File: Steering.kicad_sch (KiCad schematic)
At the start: 0 parts

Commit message: Steering: Current sensing, STM32 core, dual CAN, LEDs, test points
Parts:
- added C56, C57, C58, C61, C62, C63, C64, C65, C67, C68, C69, C70, C71, C72: 100nF, Capacitor_SMD:C_0603_1608Metric, symbol Device:C
- added C59, C66: 4.7uF, Capacitor_SMD:C_0805_2012Metric, symbol Device:C
- added C60: 1uF, Capacitor_SMD:C_0603_1608Metric, symbol Device:C
- added C73, C74, C75, C76: 22pF, Capacitor_SMD:C_0603_1608Metric, symbol Device:C
- added C85: 100nF, symbol Device:C
- added C86: 100nF, Package_SO:SOIC-8_3.9x4.9mm_P1.27mm, symbol Device:C
- added C87: 220uF, symbol Device:C
- added D11, D13, D14, D15: LED, LED_THT:LED_D3.0mm, symbol Device:LED
- added D12: LED, Resistor_SMD:R_0603_1608Metric, symbol Device:LED
- added FB2: 600R@100MHz, Inductor_SMD:L_0603_1608Metric, symbol Device:FerriteBead_Small
- added J10: Conn_01x03, Connector_PinHeader_2.54mm:PinHeader_1x03_P2.54mm_Vertical, symbol Connector_Generic:Conn_01x03
- added J11: SWD, Connector_PinHeader_2.54mm:PinHeader_1x06_P2.54mm_Vertical, symbol Connector_Generic:Conn_01x06
- added J12: SERVO, Connector:Tag-Connect_TC2030-IDC-FP_2x03_P1.27mm_Vertical, symbol Connector_Generic:Conn_01x03
- added J13: Conn_01x13, Connector:Tag-Connect_TC2030-IDC-FP_2x03_P1.27mm_Vertical, symbol Connector_Generic:Conn_01x13
- added R39, R43, R46, R47, R48, R49: 10k, Resistor_SMD:R_0603_1608Metric, symbol Device:R
- added R40, R41, R42, R44, R45: 220, Resistor_SMD:R_0603_1608Metric, symbol Device:R
- added R50, R51: 120R, Resistor_SMD:R_0603_1608Metric, symbol Device:R
- added R52: 50m, Resistor_SMD:R_Shunt_Vishay_WSK2512_6332Metric_T1.19mm, symbol Device:R_Shunt
- added R58: 1k, Package_SO:TSSOP-20_4.4x6.5mm_P0.65mm, symbol Device:R
- added SW10: SW_Push, Button_Switch_THT:SW_PUSH_6mm, symbol Switch:SW_Push
- added SW11, SW12: 219-2MSTR, Button_Switch_SMD:SW_DIP_SPSTx02_Slide_6.7x6.64mm_W8.61mm_P2.54mm_LowProfile, symbol Switch:SW_DIP_x02
- added SW13, SW14: CVS-01TB, Button_Switch_SMD:SW_DIP_SPSTx01_Slide_Copal_CVS-01xB_W5.9mm_P1mm, symbol Switch:SW_DIP_x01
- added TP21: TestPoint, Package_TO_SOT_SMD:SOT-23-5, symbol Connector:TestPoint
- added U13: STM32F401RETx, Package_QFP:LQFP-64_10x10mm_P0.5mm, symbol MCU_ST_STM32F4:STM32F401RETx
- added U14, U15: MCP2515T-I/ST, Package_SO:TSSOP-20_4.4x6.5mm_P0.65mm, symbol Interface_CAN_LIN:MCP2515-xST
- added U16, U17: SN65HVD230, Package_SO:SOIC-8_3.9x4.9mm_P1.27mm, symbol Interface_CAN_LIN:SN65HVD230
- added U18: INA180A1, Package_TO_SOT_SMD:SOT-23-5, symbol Amplifier_Current:INA180A1
- added Y5, Y6: 16 MHz, Crystal:Crystal_SMD_3225-4Pin_3.2x2.5mm, symbol Device:Crystal_GND24
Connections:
- new net: U15.1 (TXCAN), U17.1 (D)
- new net: U15.2 (RXCAN), U17.4 (R)
- new net: SW12.2, U17.6 (CANL)
- new net: SW12.1, U17.7 (CANH)
- new net: R49.2, U17.8 (Rs)
- new net: R43.1, U13.60 (BOOT0)
- new net: C70.1, R47.1, U15.19 (~{RESET})
- new net: D13.2 (A), R42.2
- new net: R50.1, SW13.1
- new net: C57.2, C60.2, FB2.2, U13.13 (VREF+)
- new net: U14.1 (TXCAN), U16.1 (D)
- new net: U14.2 (RXCAN), U16.4 (R)
- new net: SW11.2, U16.6 (CANL)
- new net: SW11.1, U16.7 (CANH)
- new net: R48.2, U16.8 (Rs)
- new net: D12.2 (A), R41.2
- new net: C69.1, R46.1, U14.19 (~{RESET})
- new net: R51.1, SW14.1
- new net: R52.2, U18.3 (+)
- new net: R52.3, U18.4 (-)
- new net: D14.2 (A), R44.2
- new net: D11.2 (A), R40.2
- new net: C59.2, U13.30 (VCAP1)
- new net: D15.2 (A), R45.2
- new net +6V: C87.1, R52.1
- new net 3V3: C61.2, C62.2, C63.2, C64.1, C65.1, C66.1, C67.1, C68.1, C71.1, C72.1, C86.1, FB2.1, J11.1 (Pin_1), R39.1, R46.2, R47.2, U13.1 (VBAT), U13.19 (VDD), U13.32 (VDD), U13.48 (VDD), U13.64 (VDD), U14.20 (VDD), U15.20 (VDD), U16.3 (VCC), U17.3 (VCC), U18.5 (V+)
- new net CANH_A: R50.2, SW11.4
- new net CANH_B: R51.2, SW12.4
- new net CANL_A: SW11.3, SW13.2
- new net CANL_B: SW12.3, SW14.2
- new net GND: C56.2, C57.1, C58.1, C59.1, C60.1, C61.1, C62.1, C63.1, C64.2, C65.2, C66.2, C67.2, C68.2, C69.2, C70.2, C71.2, C72.2, C73.2, C74.2, C75.2, C76.2, C85.2, C86.2, C87.2, D11.1 (K), D12.1 (K), D13.1 (K), D14.1 (K), D15.1 (K), J10.3 (Pin_3), J11.3 (Pin_3), J12.3 (Pin_3), J13.1 (Pin_1), J13.2 (Pin_2), R43.2, R48.1, R49.1, SW10.1, U13.12 (VSSA), U13.18 (VSS), U13.31 (VSS), U13.47 (VSS), U13.63 (VSS), U14.10 (VSS), U15.10 (VSS), U16.2 (GND), U17.2 (GND), U18.2 (GND), Y5.2 (G), Y5.4 (G), Y6.2 (G), Y6.4 (G)
- new net OSC_ST_A1: C73.1, U14.9 (OSC1), Y5.1
- new net OSC_ST_A2: C75.1, U14.8 (OSC2), Y5.3
- new net OSC_ST_B1: C74.1, U15.8 (OSC2), Y6.1
- new net OSC_ST_B2: C76.1, U15.9 (OSC1), Y6.3
- new net RELAY_TX: J13.12 (Pin_12), U13.42 (PA9)
- new net SERVO_ISENSE: C85.1, R58.2, U13.9 (PC1)
- new net SERVO_PWM: J12.2 (Pin_2)
- new net SERVO_V+: J12.1 (Pin_1), R52.4
- new net SRV: J13.9 (Pin_9), U13.62 (PB9)
- new net ST_CAN_A_CS: U13.58 (PB6), U14.18 (~{CS})
- new net ST_CAN_A_INT: U13.43 (PA10), U14.13 (~{INT})
- new net ST_CAN_B_CS: U13.38 (PC7), U15.18 (~{CS})
- new net ST_CAN_B_INT: U13.57 (PB5), U15.13 (~{INT})
- new net ST_CAN_RX_A: J13.3 (Pin_3), U13.10 (PC2)
- new net ST_CAN_RX_B: J13.4 (Pin_4), U13.11 (PC3)
- new net ST_CAN_TX_A: J13.5 (Pin_5), U13.51 (PC10)
- new net ST_CAN_TX_B: J13.6 (Pin_6), U13.52 (PC11)
- new net ST_DEG_A: J13.7 (Pin_7), R41.1, U13.61 (PB8)
- new net ST_DEG_B: J13.8 (Pin_8), R40.1, U13.8 (PC0)
- new net ST_ERR: J13.13 (Pin_13), R42.1, U13.53 (PC12), U13.55 (PB3)
- new net ST_FL: J13.10 (Pin_10), R44.1, U13.29 (PB10)
- new net ST_FR: J13.11 (Pin_11), R45.1, U13.41 (PA8)
- new net ST_NRST: C58.2, J11.5 (Pin_5), U13.7 (NRST)
- new net ST_SELF_TEST: C56.1, R39.2, SW10.2, U13.2 (PC13)
- new net ST_SPI_MISO: U13.22 (PA6), U14.17 (SO), U15.17 (SO)
- new net ST_SPI_MOSI: U13.23 (PA7), U14.16 (SI), U15.16 (SI)
- new net ST_SPI_SCLK: U13.21 (PA5), U14.14 (SCK), U15.14 (SCK)
- new net ST_SWCLK: J11.2 (Pin_2), U13.49 (PA14)
- new net ST_SWDIO: J11.4 (Pin_4), U13.46 (PA13)
- new net ST_SWO: J11.6 (Pin_6), U13.56 (PB4)
- new net ST_UART_RX: J10.1 (Pin_1), U13.17 (PA3)
- new net ST_UART_TX: J10.2 (Pin_2), U13.16 (PA2)
- new net TP_SERVO_ISENSE: R58.1, TP21.1, U18.1
- no-connect marks 0 -> 38
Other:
- note added: "CAN A Interface"
- note added: "CAN B Interface"
- note added: "Connectors & Test Points"
- note added: "Current Sensing"
- note added: "I_mA = counts * 0.806 - offset Sample rate @ >=10KHz"
- note added: "Kelvin"
- note added: "Low ESR"
- note added: "STM Breakout"

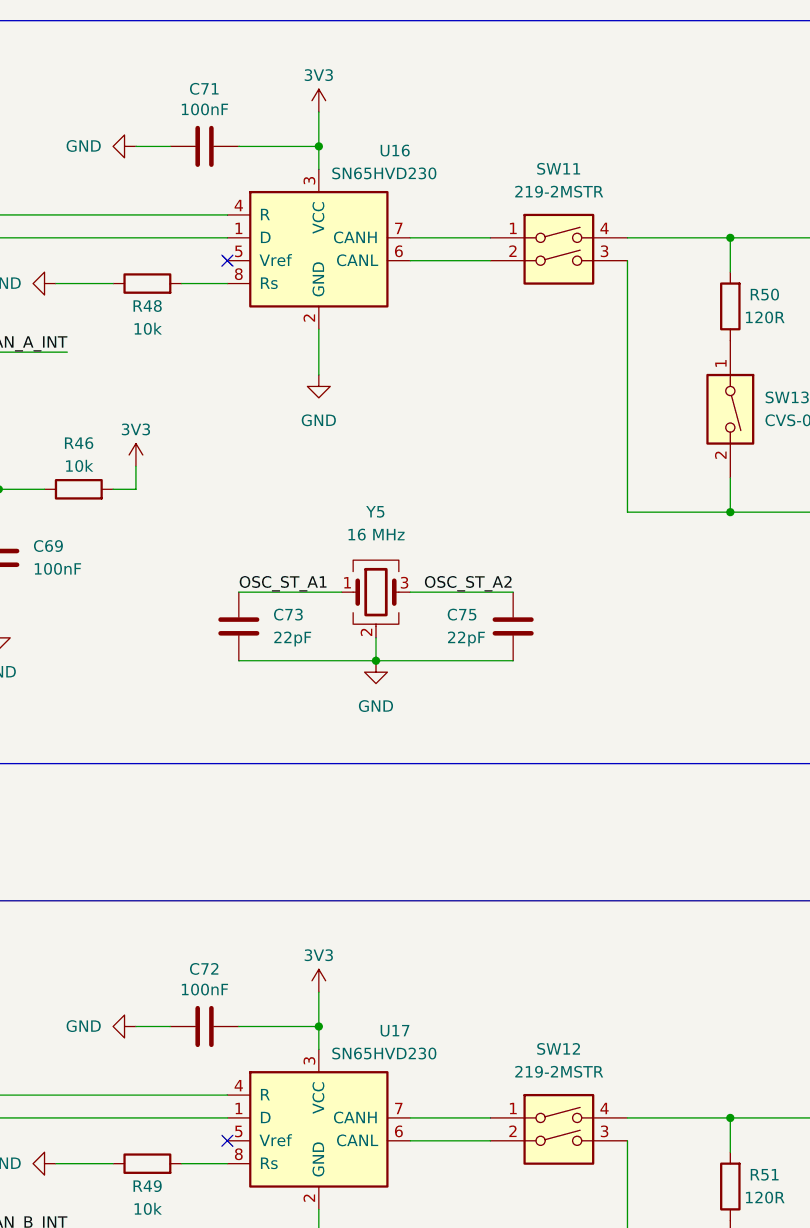
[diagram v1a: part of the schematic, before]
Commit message: changed MPN on CAN
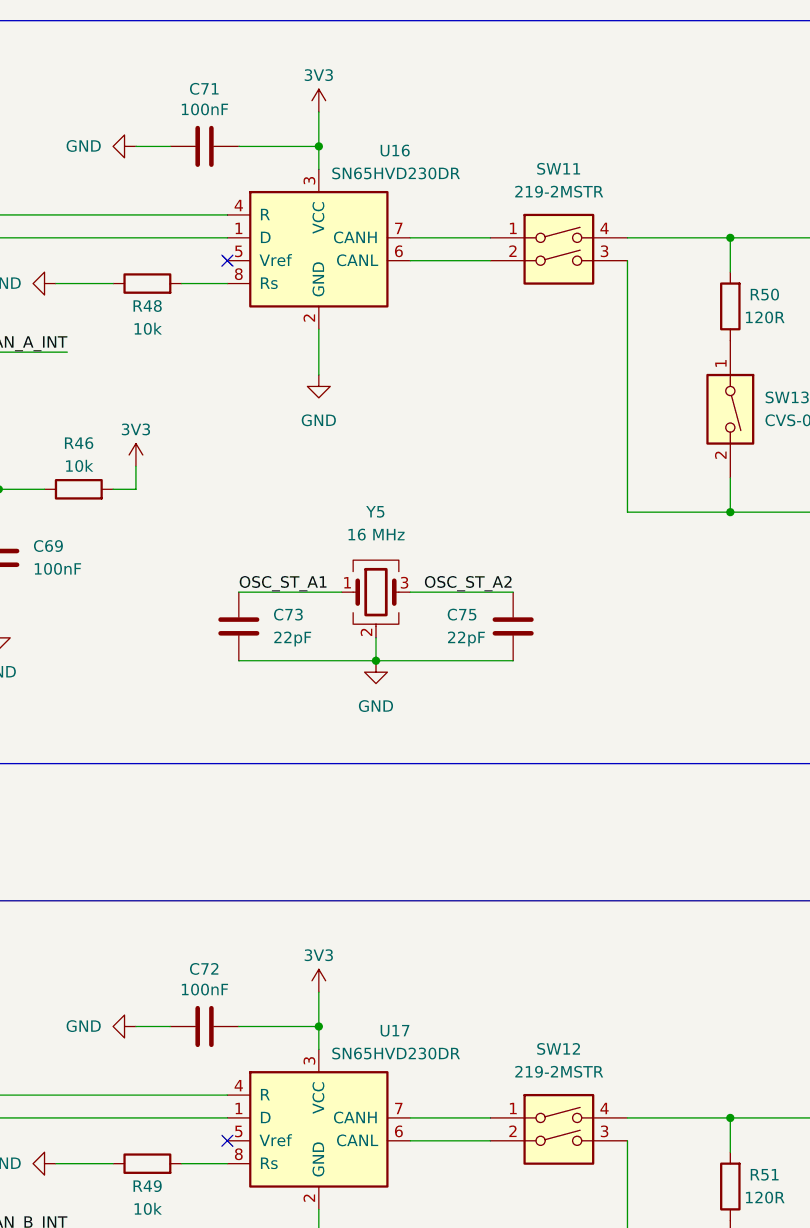
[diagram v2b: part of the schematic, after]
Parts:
- U16, U17: value SN65HVD230 -> SN65HVD230DR; Assembly (none) -> SMT; JLCPCB Category (none) -> Extended; LCSC Part # (none) -> C12084; Manufacturer (none) -> Texas Instruments; Manufacturer Part Number (none) -> SN65HVD230DR; Source (none) -> JLCPCB

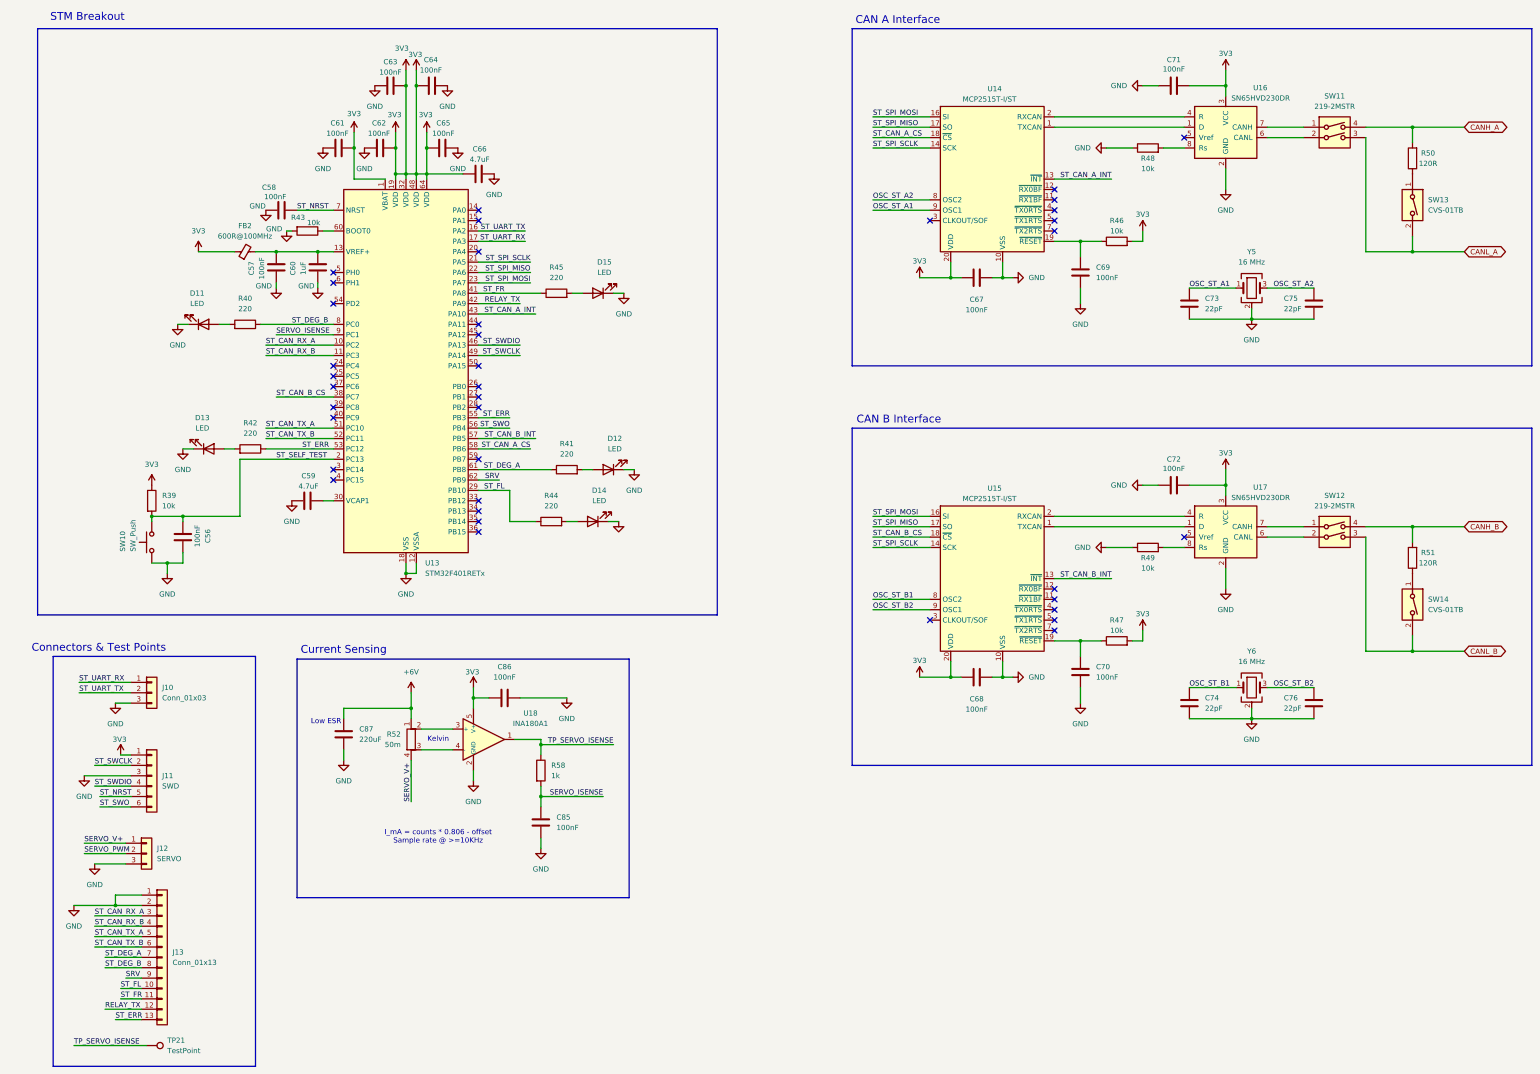
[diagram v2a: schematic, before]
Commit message: Re-annotate whole schematic (sheet x100); drivetrain SCLK fix, BOM fields, footprints
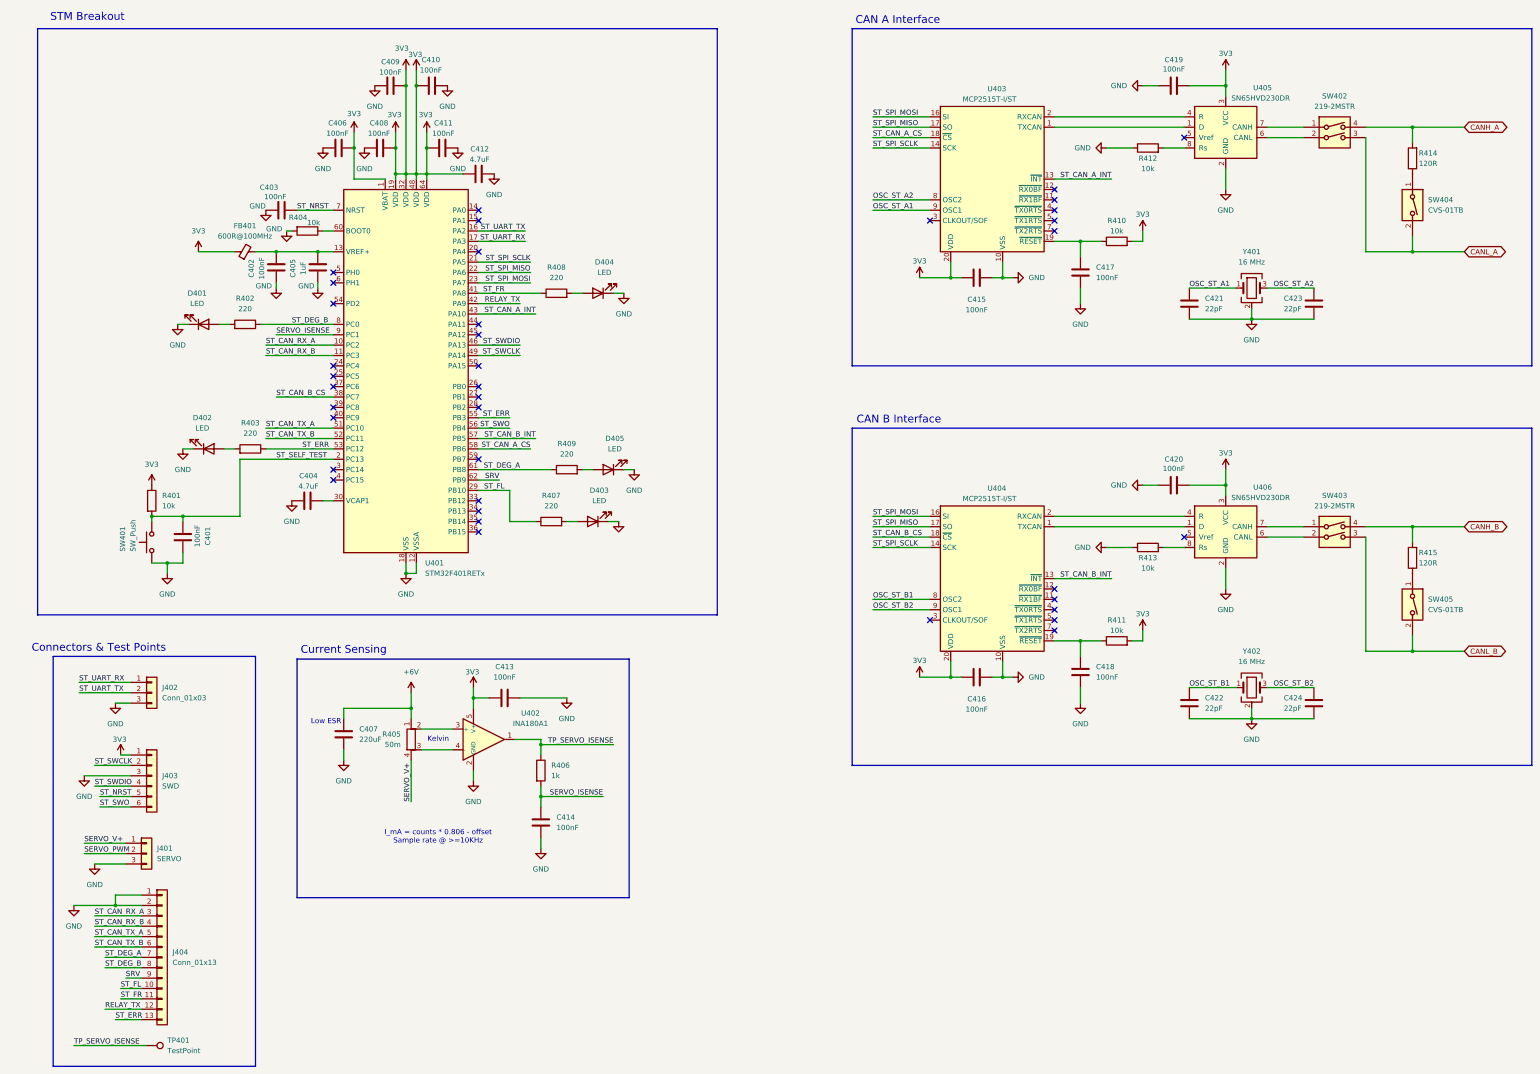
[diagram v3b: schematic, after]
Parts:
- renumbered C56 to C401, C57 to C402, C58 to C403, C59 to C404, C60 to C405, C61 to C406, C87 to C407, C62 to C408, C63 to C409, C64 to C410, C65 to C411, C66 to C412, C86 to C413, C85 to C414, C67 to C415, C68 to C416, C69 to C417, C70 to C418, C71 to C419, C72 to C420, C73 to C421, C74 to C422, C75 to C423, C76 to C424, D11 to D401, D13 to D402, D14 to D403, D15 to D404, D12 to D405, FB2 to FB401, J12 to J401, J10 to J402, J11 to J403, J13 to J404, R39 to R401, R40 to R402, R42 to R403, R43 to R404, R52 to R405, R58 to R406, R44 to R407, R45 to R408, R41 to R409, R46 to R410, R47 to R411, R48 to R412, R49 to R413, R50 to R414, R51 to R415, SW10 to SW401, SW11 to SW402, SW12 to SW403, SW13 to SW404, SW14 to SW405, TP21 to TP401, U13 to U401, U18 to U402, U14 to U403, U15 to U404, U16 to U405, U17 to U406, Y5 to Y401, Y6 to Y402

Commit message: Added library components for steering; fixed conflicting pins and pin order
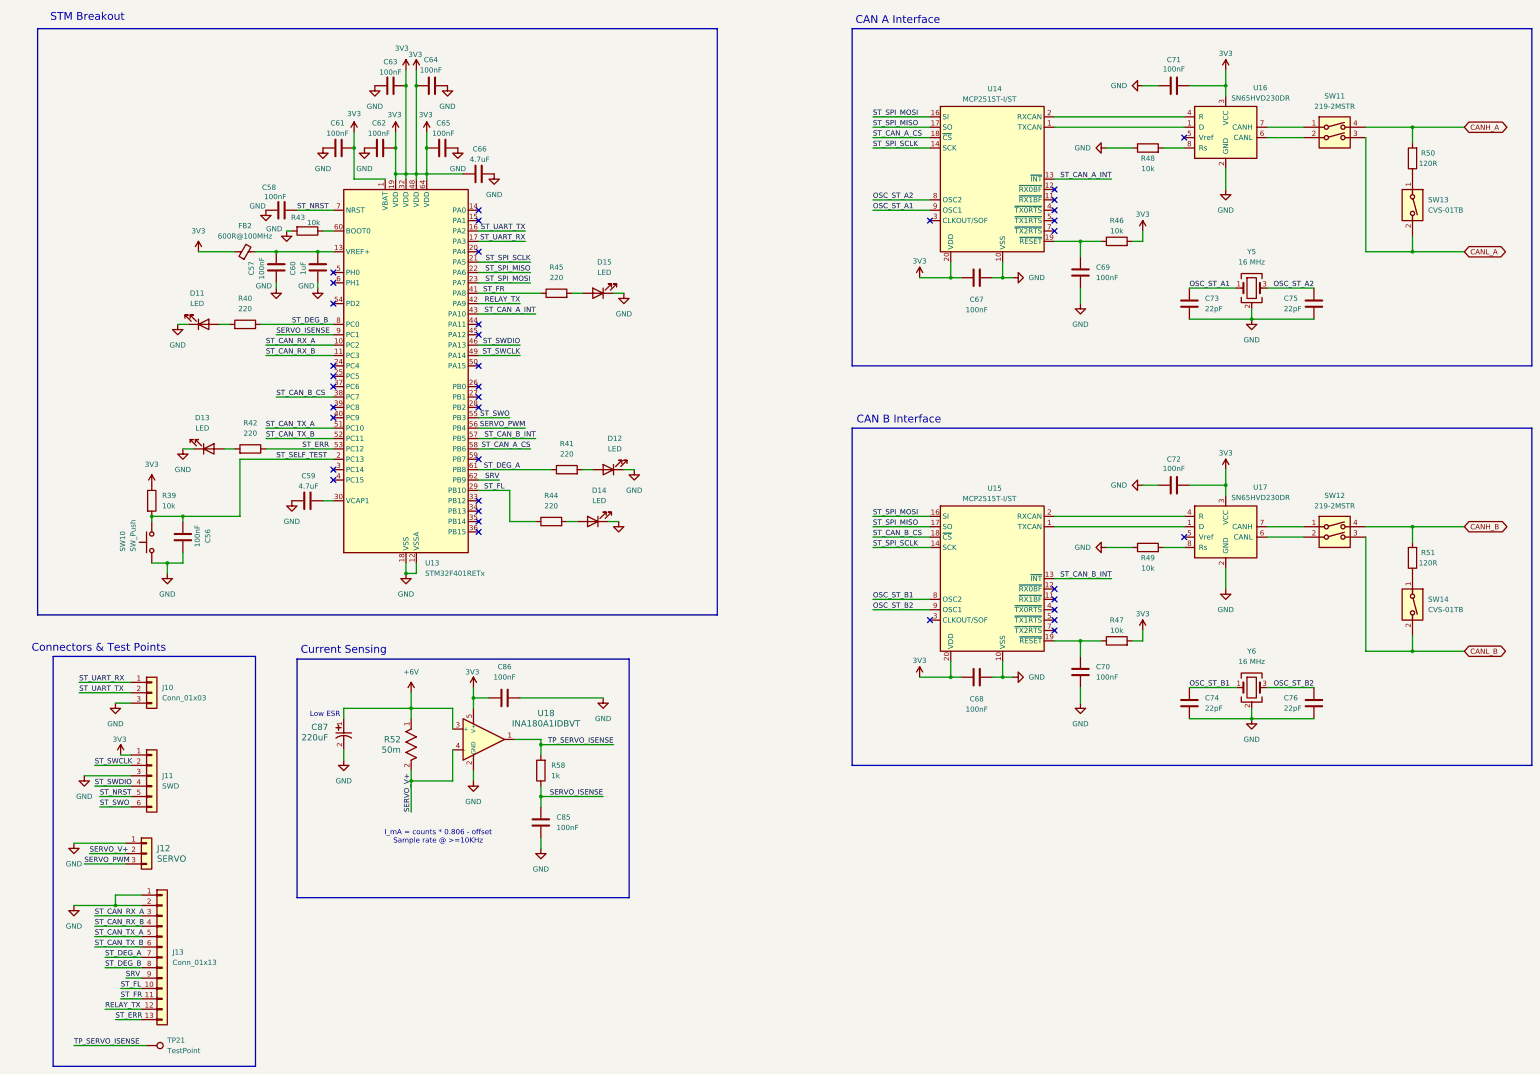
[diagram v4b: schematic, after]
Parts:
- removed C407: 220uF, symbol Device:C
- removed C413: 100nF, Package_SO:SOIC-8_3.9x4.9mm_P1.27mm, symbol Device:C
- removed C414: 100nF, symbol Device:C
- removed J401: SERVO, Connector:Tag-Connect_TC2030-IDC-FP_2x03_P1.27mm_Vertical, symbol Connector_Generic:Conn_01x03
- removed R405: 50m, Resistor_SMD:R_Shunt_Vishay_WSK2512_6332Metric_T1.19mm, symbol Device:R_Shunt
- removed R406: 1k, Package_SO:TSSOP-20_4.4x6.5mm_P0.65mm, symbol Device:R
- removed U402: INA180A1, Package_TO_SOT_SMD:SOT-23-5, symbol Amplifier_Current:INA180A1
- added C85, C86: 100nF, Capacitor_SMD:C_0603_1608Metric, symbol Device:C
- added C87: 220uF, EEE-FK1C221P:CAP_EEFK_E_PAN-M, symbol EEE-FK1C221P:EEE-FK1C221P
- added J12: SERVO, 39301039:CONN_55660330-SD_MOL, symbol Connector_Generic:Conn_01x03
- added R52: 50m, WSL2512R0500FEA:RES_2512_WSL-M, symbol WSL2512R0500FEA:WSL2512R0500FEA
- added R58: 1k, Resistor_SMD:R_0603_1608Metric, symbol Device:R
- added U18: INA180A1IDBVT, INA180A1IDBVT:DBV0005A_M, symbol Amplifier_Current:INA180A1
- J13: renamed from J404; footprint Connector:Tag-Connect_TC2030-IDC-FP_2x03_P1.27mm_Vertical -> Connector_PinHeader_2.54mm:PinHeader_1x13_P2.54mm_Vertical
- TP21: renamed from TP401; footprint Package_TO_SOT_SMD:SOT-23-5 -> TestPoint:TestPoint_Keystone_5015_Micro_Mini
- renumbered C401 to C56, C402 to C57, C403 to C58, C404 to C59, C405 to C60, C406 to C61, C408 to C62, C409 to C63, C410 to C64, C411 to C65, C412 to C66, C415 to C67, C416 to C68, C417 to C69, C418 to C70, C419 to C71, C420 to C72, C421 to C73, C422 to C74, C423 to C75, C424 to C76, D401 to D11, D405 to D12, D402 to D13, D403 to D14, D404 to D15, FB401 to FB2, J402 to J10, J403 to J11, R401 to R39, R402 to R40, R409 to R41, R403 to R42, R404 to R43, R407 to R44, R408 to R45, R410 to R46, R411 to R47, R412 to R48, R413 to R49, R414 to R50, R415 to R51, SW401 to SW10, SW402 to SW11, SW403 to SW12, SW404 to SW13, SW405 to SW14, U401 to U13, U403 to U14, U404 to U15, U405 to U16, U406 to U17, Y401 to Y5, Y402 to Y6
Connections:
- net +6V: now also C87.1, R52.1, U18.3 (+)
- net 3V3: now also C86.1, U18.5 (V+)
- net GND: now also C85.2, C86.2, C87.2, J12.1 (Pin_1), U18.2 (GND)
- net SERVO_ISENSE: now also C85.1, R58.1
- net SERVO_PWM: now also U13.56 (PB4), J12.3 (Pin_3)
- net SERVO_V+: now also J12.2 (Pin_2), R52.2, U18.4 (-)
- net ST_ERR: no longer U13.55 (PB3)
- net ST_SWO: now also U13.55 (PB3); no longer U13.56 (PB4)
- net TP_SERVO_ISENSE: now also R58.2, U18.1
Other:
- note removed: "Kelvin"
